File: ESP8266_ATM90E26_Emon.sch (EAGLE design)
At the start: 96 parts, among them IC1 CP2104, IC2 RTC_PCF8523T, J2 ST-PJ-312, J4 12V AC, Q1 mmbt2222, Q2 mmbt2222, Q3 8.192MHz, SW2 KMR2, U1 ATM90E26, U2 SPX3819, U3 MCP73831T-2ACI/OT, U4 CJT1117-5.0-SOT223, X1 JSTPH, X2 ESP-12, X3 microsd, X4 20329, Y1 32khz

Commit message: Pulled parts into 50x50mm dimension
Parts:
- LOGO1: value OSHW-LOGOM -> OSHW-LOGOS; device SparkFun-Aesthetics:OSHW-LOGOM -> SparkFun-Aesthetics:OSHW-LOGOS
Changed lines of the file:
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@@
 <?xml version="1.0" encoding="utf-8"?>
 <!DOCTYPE eagle SYSTEM "eagle.dtd">
-<eagle version="7.4.0">
+<eagle version="7.6.0">
 <drawing>
 <settings>
@@
 <part name="SJ1" library="microbuilder" deviceset="SOLDERJUMPER_CLOSED" device=""/>
 <part name="FRAME2" library="SparkFun-Aesthetics" deviceset="FRAME-A4L" device=""/>
-<part name="LOGO1" library="SparkFun-Aesthetics" deviceset="OSHW-LOGO" device="M"/>
+<part name="LOGO1" library="SparkFun-Aesthetics" deviceset="OSHW-LOGO" device="S" value="OSHW-LOGOS"/>
 <part name="J4" library="dp_devices" deviceset="CON_DC_M" device="-DC_SMD" value="12V AC"/>
 <part name="R21" library="Seeed-Resistor-2016" deviceset="SMD-RES-0R(0603)" device="" value="100K"/>

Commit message: Some signal renaming
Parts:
- C2, C23, C3, C6, C8: device microbuilder:CAP_CERAMIC0805-NOOUTLINE -> microbuilder:CAP_CERAMIC0603_NO
- CHG: device microbuilder:LED0805_NOOUTLINE -> microbuilder:LED0603_NOOUTLINE
- INT1: device microbuilder:HEADER-1X1ROUND -> microbuilder:HEADER-1X1-SMD-MASKHELD_1X2MM
- R24, R25: device microbuilder:RESISTOR0805_NOOUTLINE -> microbuilder:RESISTOR_0603_NOOUT
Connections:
- removed net +3V3: C1.+, C23.1, C9.1, IC2.VDD, MMD0-0R.1, MMD1-0R.3, R12.2, R24.2, R25.2, U1.!RESET, U1.DVDD, USEL-0R.1, X3.SD_VDD
- removed net N$9: MMD1-0R.2, U1.MMD1
- removed net USB: D2.-, R23.1
- net 3.3V: now also C1.+, C23.1, C9.1, IC2.VDD, MMD0-0R.1, MMD1-0R.2, MMD1-0R.3, R12.2, R24.2, R25.2, U1.!RESET, U1.DVDD, U1.MMD1, USEL-0R.1, X3.SD_VDD
- net VBUS: now also D2.-, R23.1

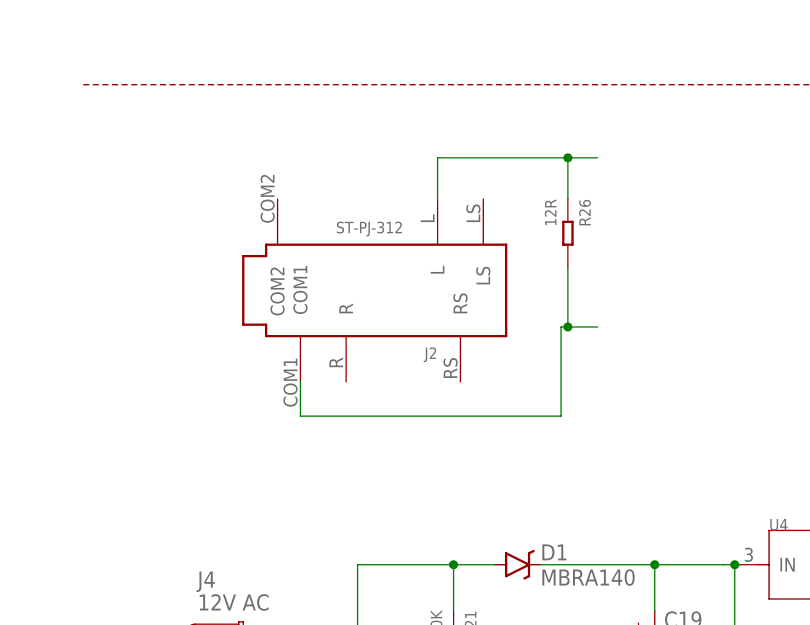
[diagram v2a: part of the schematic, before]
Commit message: Squeeze all parts into 50x50mm
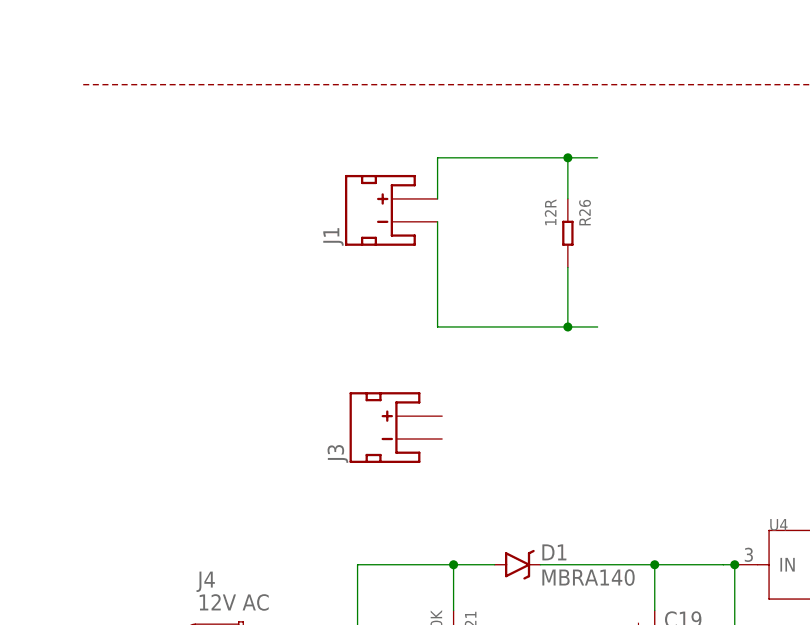
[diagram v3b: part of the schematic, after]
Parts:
- removed J2: ST-PJ-312, Seeed-OPL-Connector:AUDIO-JACK-6P-SMD(ST-PJ-312)
- added J1, J3: (no value), SparkFun-Connectors:JST_2MM_MALE
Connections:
- net I1N_IN1: now also J1.-; no longer J2.COM1
- net I1P_IN1: now also J1.+; no longer J2.L
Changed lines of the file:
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@@
 <part name="C21" library="Discrete" deviceset="C*" device="-0603" value="100n"/>
 <part name="C22" library="Discrete" deviceset="C*" device="-0603" value="100n"/>
-<part name="J2" library="Seeed-OPL-Connector" deviceset="AUDIO-JACK-6P-SMD(ST-PJ-312)" device="" value="ST-PJ-312"/>
 <part name="CF1" library="wirepad" deviceset="WIREPAD" device="SMD1,27-254" value="WIREPADSMD1,27-254"/>
 <part name="U1" library="ATM90E26" deviceset="ATM90E26" device=""/>
@@
 <part name="U$25" library="microbuilder" deviceset="3.3V" device=""/>
 <part name="U$26" library="microbuilder" deviceset="3.3V" device=""/>
+<part name="J1" library="SparkFun-Connectors" deviceset="JST_2MM_MALE" device=""/>
+<part name="J3" library="SparkFun-Connectors" deviceset="JST_2MM_MALE" device=""/>
 </parts>
 <sheets>
@@
 <instance part="C21" gate="C" x="110.49" y="105.41" rot="R90"/>
 <instance part="C22" gate="C" x="133.35" y="105.41" rot="R90"/>
-<instance part="J2" gate="G$1" x="71.12" y="147.32" rot="R180"/>
 <instance part="CF1" gate="G$1" x="134.62" y="198.12" smashed="yes" rot="R180">
 <attribute name="NAME" x="132.969" y="199.8218" size="1.778" layer="95" rot="R180"/>
@@
 <instance part="U$25" gate="G$1" x="299.72" y="231.14"/>
 <instance part="U$26" gate="G$1" x="276.86" y="228.6"/>
+<instance part="J1" gate="G$1" x="72.39" y="154.94" rot="R90"/>
+<instance part="J3" gate="G$1" x="72.898" y="130.81" rot="R90"/>
 </instances>
 <busses>
@@
 <wire x1="77.47" y1="157.48" x2="77.47" y2="162.052" width="0.1524" layer="91"/>
 <wire x1="77.47" y1="162.052" x2="91.948" y2="162.052" width="0.1524" layer="91"/>
-<pinref part="J2" gate="G$1" pin="L"/>
 <wire x1="91.948" y1="162.052" x2="95.25" y2="162.052" width="0.1524" layer="91"/>
 <wire x1="91.948" y1="162.052" x2="91.948" y2="157.48" width="0.1524" layer="91"/>
 <junction x="91.948" y="162.052"/>
 <pinref part="R26" gate="G$1" pin="1"/>
+<pinref part="J1" gate="G$1" pin="+"/>
 </segment>
 </net>
 <net name="I1N_IN1" class="0">
 <segment>
-<wire x1="62.23" y1="137.16" x2="62.23" y2="133.35" width="0.1524" layer="91"/>
-<wire x1="62.23" y1="133.35" x2="91.186" y2="133.35" width="0.1524" layer="91"/>
-<wire x1="91.186" y1="133.35" x2="91.186" y2="143.256" width="0.1524" layer="91"/>
-<wire x1="91.186" y1="143.256" x2="91.948" y2="143.256" width="0.1524" layer="91"/>
-<pinref part="J2" gate="G$1" pin="COM1"/>
 <pinref part="R26" gate="G$1" pin="2"/>
 <wire x1="91.948" y1="143.256" x2="95.25" y2="143.256" width="0.1524" layer="91"/>
 <wire x1="91.948" y1="149.86" x2="91.948" y2="143.256" width="0.1524" layer="91"/>
 <junction x="91.948" y="143.256"/>
-</segment>
-</net>
+<pinref part="J1" gate="G$1" pin="-"/>
+<wire x1="91.948" y1="143.256" x2="77.47" y2="143.256" width="0.1524" layer="91"/>
+<wire x1="77.47" y1="143.256" x2="77.47" y2="154.94" width="0.1524" layer="91"/>
+</segment>
+</net>
